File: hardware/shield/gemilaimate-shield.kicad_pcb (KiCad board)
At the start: 2 copper layers, 90 x 75 mm, 38 parts, among them J1 ISOLATED 5V INPUT, J10 HEATER UNUSED, J2 ADS1115 BLUE SOCKET 1x10, J3 MAX31855 VIN SOCKET 1x6, J4 PRESSURE SENSOR, J5 ROBOTDYN EDGE DOCK 1x4, J6 SSR EDGE DOCK 1x5 USE 1-3-5, J7 CJMCU-0102 SOCKET 2x5, J8 DRY CONTACTS ONLY, J9 DISPLAY USB 5V, U1 ESP32-S3-N8R8 DevKitC-1, U2 SN74AHCT125N PDIP14, U3 SN74LVC1G17DBV SOT23-5

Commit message: Move shield J5 to bottom edge to preserve ESP32 USB access
Revise shield to v0.2.1, reserve the left USB plug corridor, and verify connector geometry against the PCB. Regenerate routing and fabrication files with zero ERC, DRC, unconnected and parity issues. Keep carrier v0.1, the component set and firmware unchanged.
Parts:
- moved J5 66.3 mm to (41.9, 71.1)
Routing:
- net /PUMP_PWM: track 50.8 -> 143.6 mm, vias 3 -> 2
- net /TC_SCK: track 50.0 -> 106.2 mm
- net /TC_CS: track 66.5 -> 119.1 mm, vias 6 -> 1
- net /HEATER_5V: track 58.7 -> 31.8 mm, vias 1 -> 0
- net /SCL_3V3: track 38.4 -> 56.9 mm, vias 0 -> 1
- net /+3V3: track 161.0 -> 178.9 mm, vias 3 -> 7
- net /+5V: track 319.3 -> 336.9 mm
- net /DEV_5V: track 29.5 -> 12.2 mm, vias 0 -> 1
- net /SDA_3V3: track 38.4 -> 53.8 mm, vias 0 -> 2
- net /GND: track 385.7 -> 399.5 mm, vias 30 -> 42
- net /PRESSURE: track 29.6 -> 15.9 mm
- net /VALVE_IN: track 52.7 -> 39.8 mm, vias 2 -> 1
- net /VALVE_5V: track 30.1 -> 17.4 mm, vias 4 -> 0
- net /SCL_5V: track 65.8 -> 54.4 mm, vias 1 -> 2
- net /ZC_RAW: track 104.1 -> 113.3 mm, vias 2 -> 4
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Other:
- board text added: "GemilaiMate v0.2.1 SHIELD - PROTOTYPE"
- board text added: "ROBOTDYN"
- board text added: "USB PLUG ACCESS - KEEP FREE"
- board text added: "github.com/Rico-X/GemilaiMate"
- board text removed: "GemilaiMate v0.2 SHIELD - PROTOTYPE"

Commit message: Apply shield assembly review and headless rebuild fixes
Revise shield to v0.2.2 with square pin-1 pads, explicit orientation labels and module outlines. Use wired controls for externally mounted RobotDyn and SSR, preserve SSR terminals, reserve mating connector and cable envelopes, move J4 for mounting clearance, and document adjustable module retention. Rebuild on Linux KiCad 10.0.7 without DISPLAY; ERC, DRC, unconnected and parity all zero. Carrier electronics and firmware remain unchanged.
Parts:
- J5: value ROBOTDYN EDGE DOCK 1x4 -> ROBOTDYN CABLE 1x4
- J6: value SSR EDGE DOCK 1x5 USE 1-3-5 -> SSR CABLE 1x5 USE 1-3-5
- J7: value CJMCU-0102 SOCKET 2x5 -> CJMCU-0102 SOCKET 2x1x5
- moved J4 1.27 mm to (8.89, 69.8)
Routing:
- net /PUMP_PWM: track 143.6 -> 97.7 mm, vias 2 -> 5
- net /SDA_5V: track 66.8 -> 54.9 mm, vias 1 -> 3
- net /PRESSURE_RAW: track 7.24 -> 5.97 mm
- net /GND: track 399.5 -> 399.7 mm, vias 42 -> 49
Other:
- board text added: "GemilaiMate v0.2.2 SHIELD - PROTOTYPE"
- board text added: "NO MAINS ON BOARD"
- board text added: "ROBOTDYN CABLE"
- board text removed: "GemilaiMate v0.2.1 SHIELD - PROTOTYPE"
- board text removed: "NO MAINS ON CARRIER"
- board text removed: "ROBOTDYN"

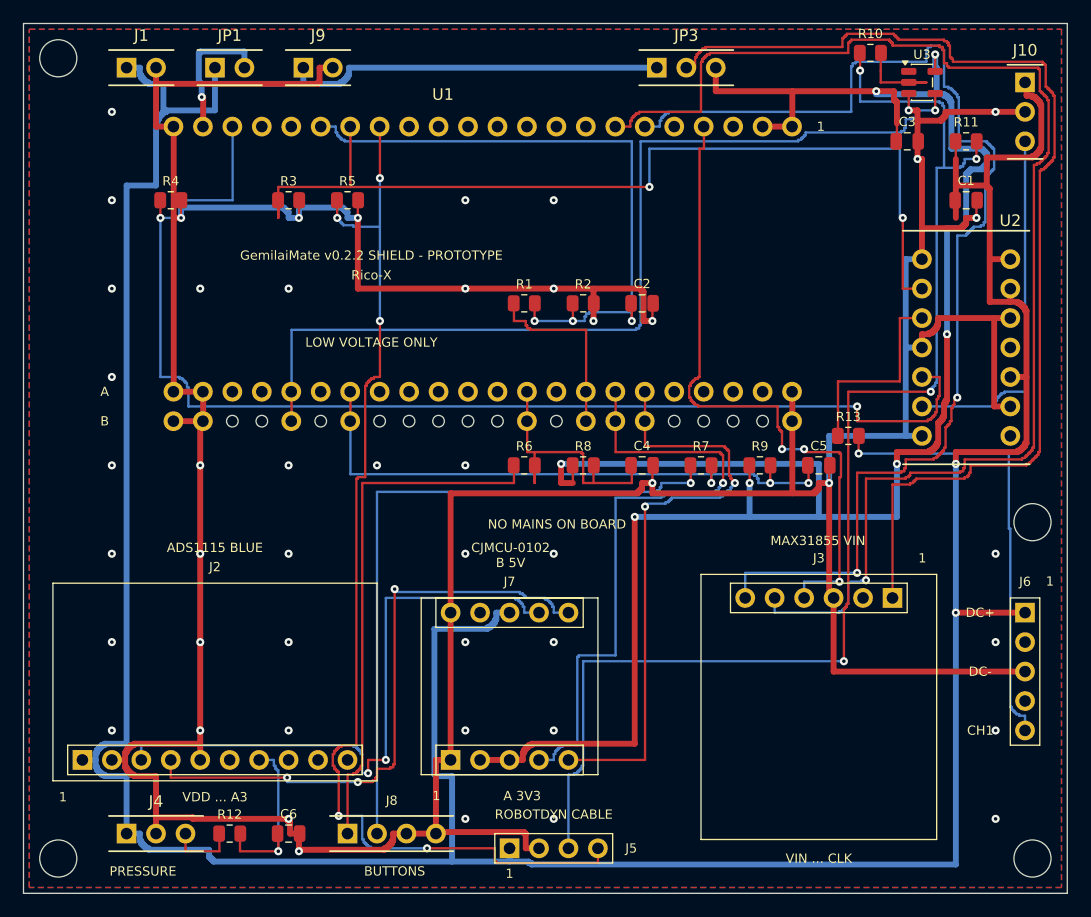
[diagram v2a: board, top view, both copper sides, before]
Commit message: Correct shield label order and specify grouped harness housings
Revise shield to v0.2.3. Match CLK/VIN words to physical pad X, place ADS/TXS labels beside their own rows, and clear selected labels from front tracks and vias. Require single marked J5/J6 harness housings for both variants and document the remaining reversal risk. Native headless rebuild, electrical checks and semantic regressions pass; copper geometry is unchanged.
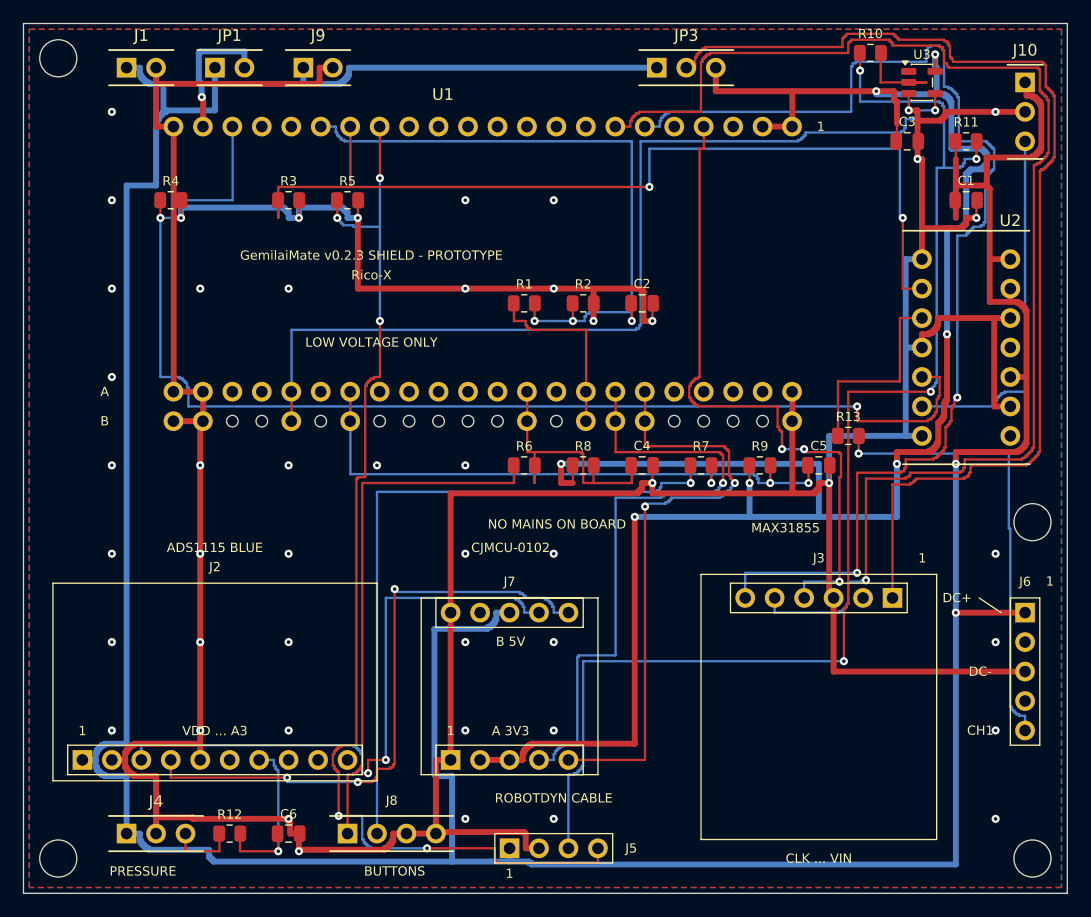
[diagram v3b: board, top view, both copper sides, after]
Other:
- board text added: "GemilaiMate v0.2.3 SHIELD - PROTOTYPE"
- board text added: "MAX31855"
- board text removed: "GemilaiMate v0.2.2 SHIELD - PROTOTYPE"
- board text removed: "MAX31855 VIN"

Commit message: Check all shield silk texts and clear remaining via overlaps
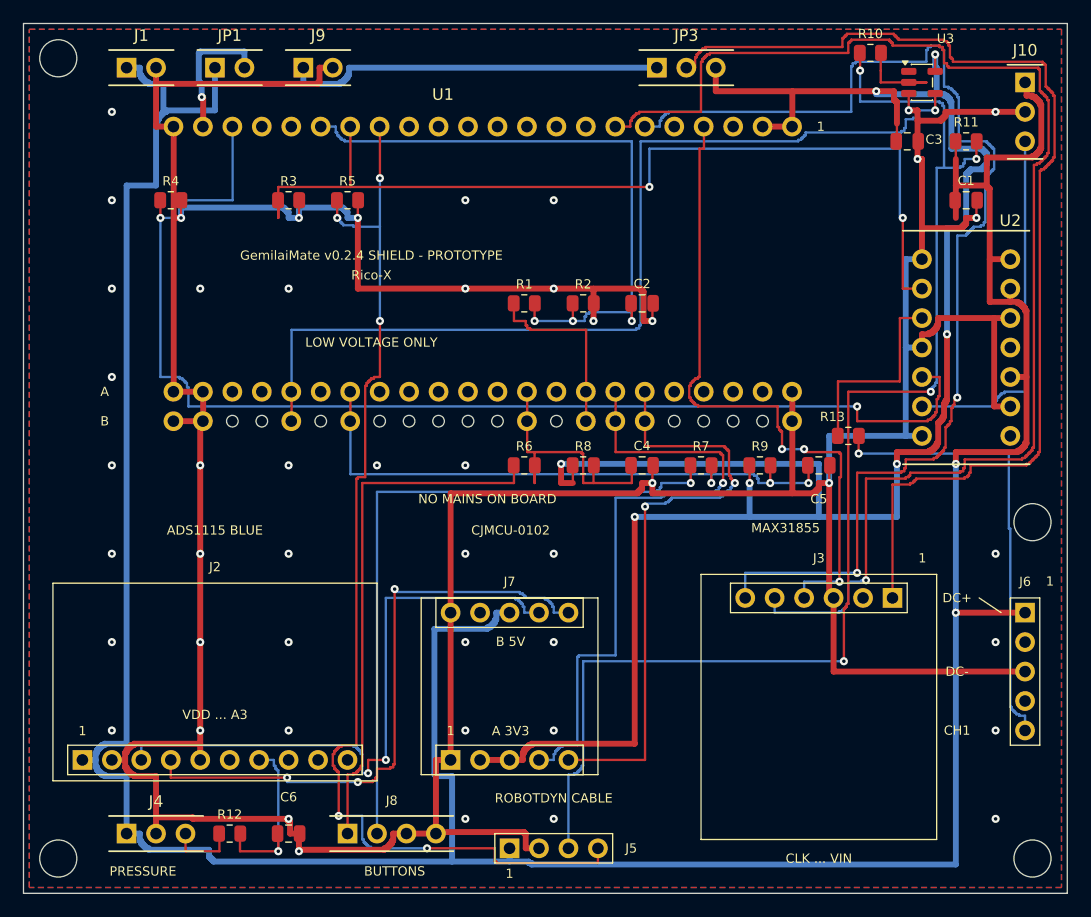
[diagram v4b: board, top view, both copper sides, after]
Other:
- board text added: "GemilaiMate v0.2.4 SHIELD - PROTOTYPE"
- board text removed: "GemilaiMate v0.2.3 SHIELD - PROTOTYPE"
